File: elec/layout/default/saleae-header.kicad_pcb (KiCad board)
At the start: 2 copper layers, 225.7 x 100.8 mm, 5 parts

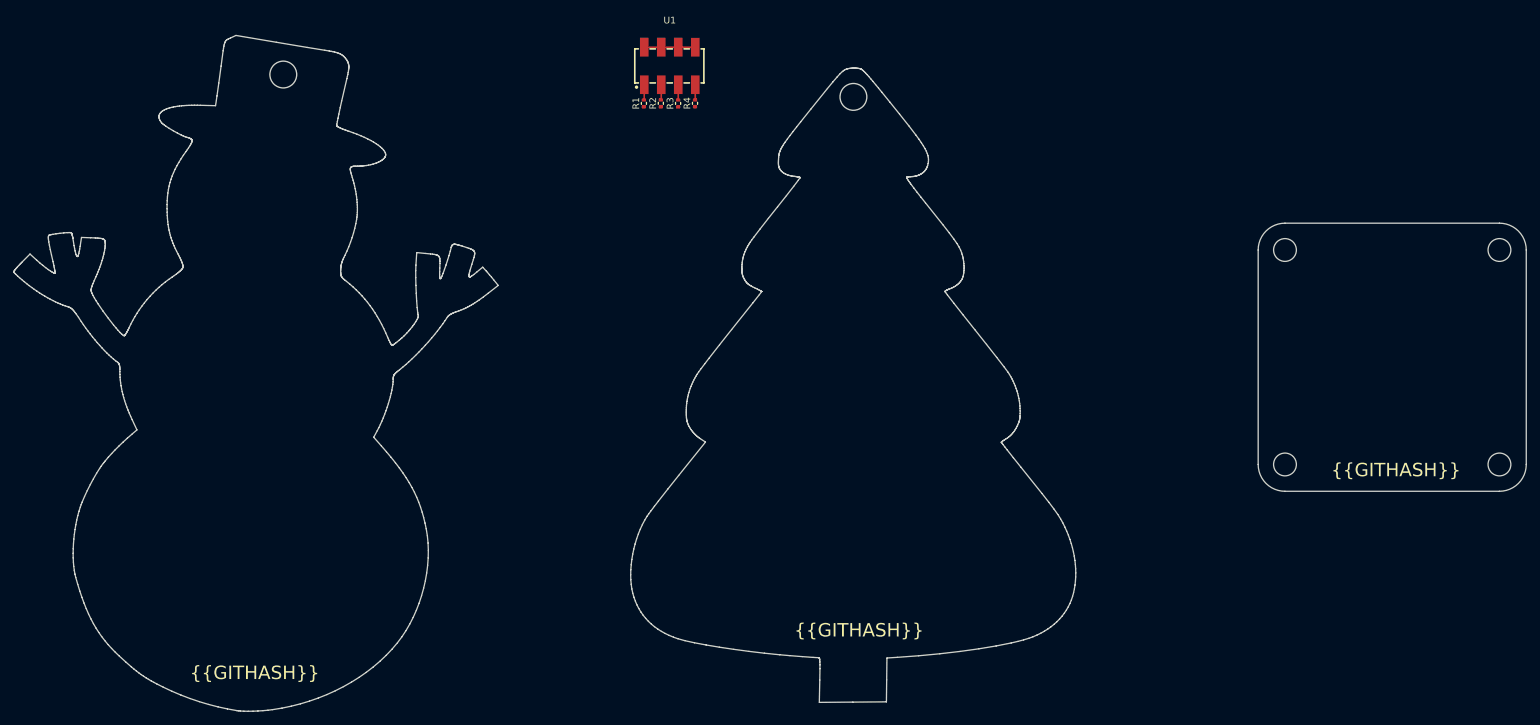
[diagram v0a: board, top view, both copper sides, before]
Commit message: Remove xmas artifacts from layout
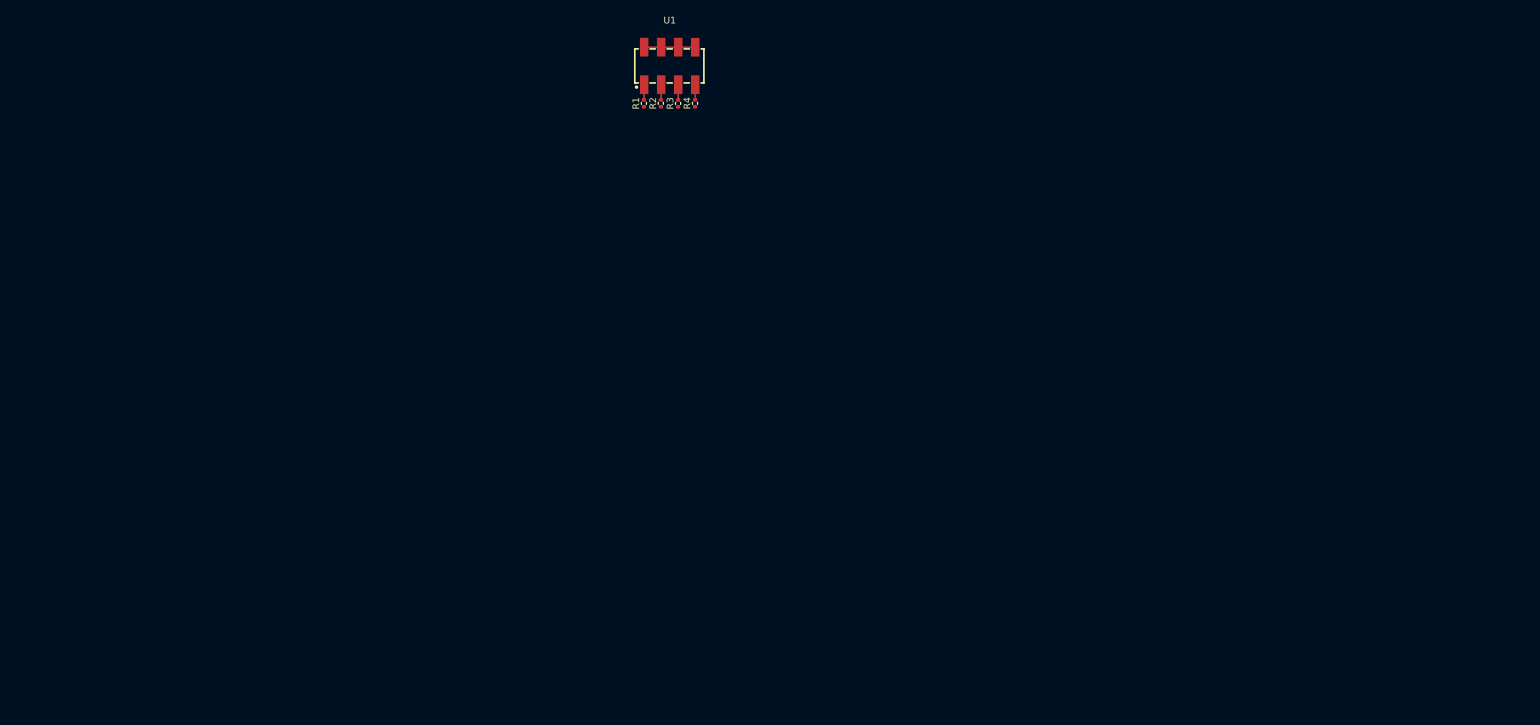
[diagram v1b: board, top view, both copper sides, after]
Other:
- board outline removed
- board text removed: "{{GITHASH}}"
